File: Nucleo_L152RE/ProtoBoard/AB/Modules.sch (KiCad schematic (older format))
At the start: 30 parts, among them CON1 USB-MICRO-B, J2 EXT, P31 Ant, U4 S25FL127S, U5 MT3329_GPS, U6 RFM69HW

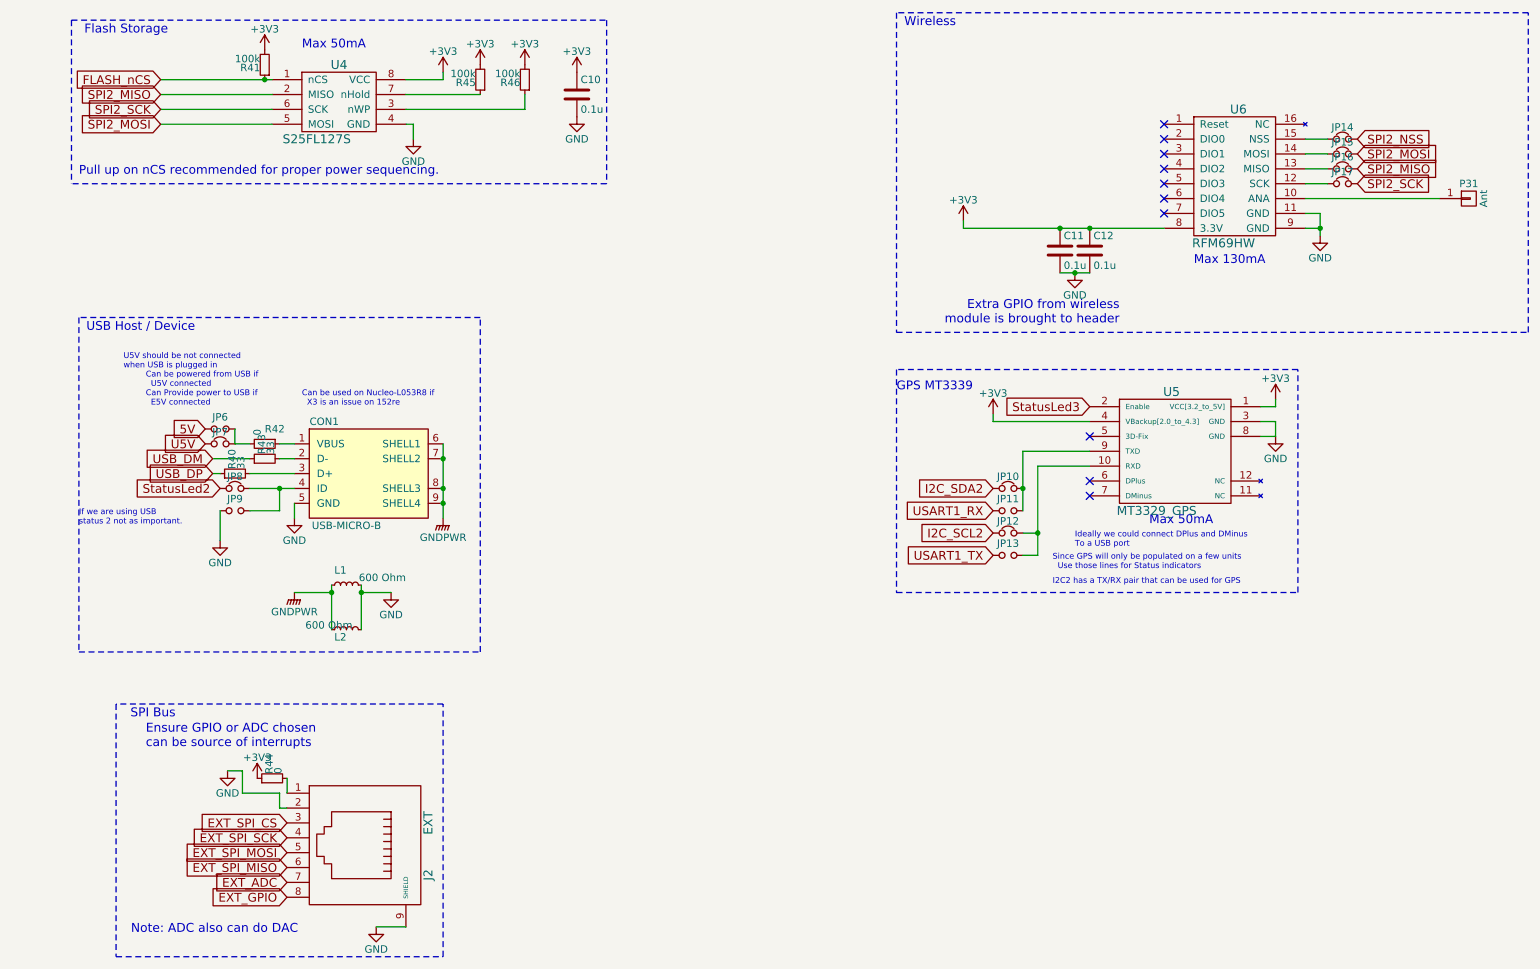
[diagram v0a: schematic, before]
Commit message: Components mostly laid out into final resting positions with exception of plethora of single pin connections for easily connecting to GND, 3.3V, 5V, 3.3Vctl.
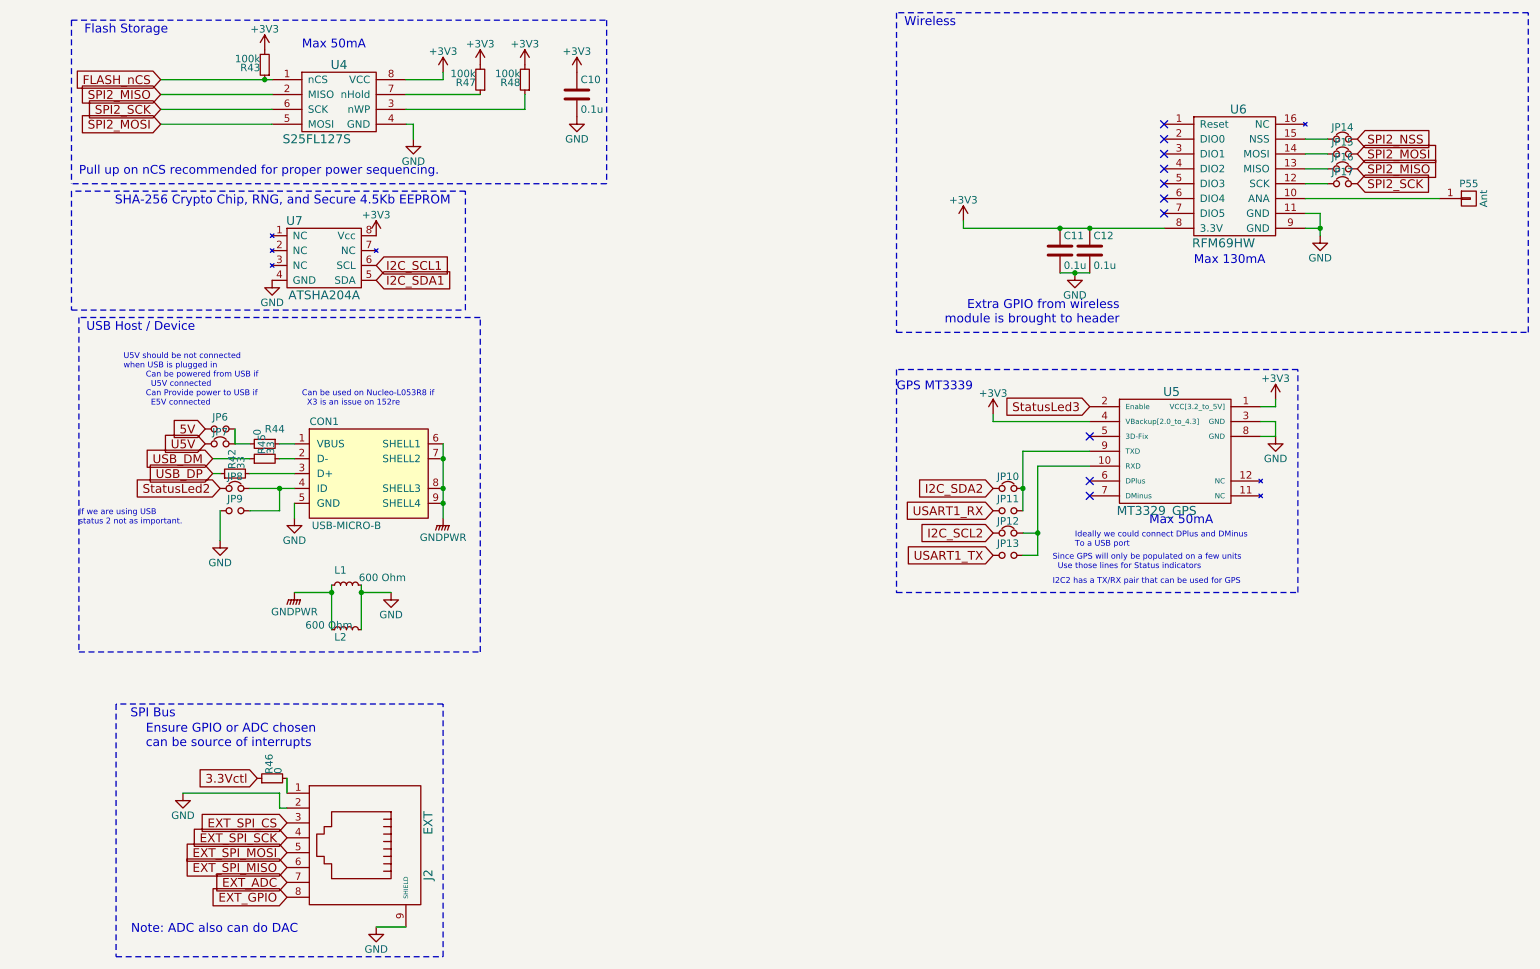
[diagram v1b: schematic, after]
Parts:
- added U7: ATSHA204A, nucleo:8-SOIC-JEDEC_MS-012AA, symbol ATSHA204A
- JP10, JP12, JP14, JP15, JP16, JP17, JP7, JP8: footprint nucleo:SB_NC -> nucleo:SB_NC_Smaller
- JP11, JP13, JP6, JP9: footprint nucleo:SB_NO -> nucleo:SB_NO_Smaller
- P55: renamed from P31; footprint Pin_Headers:Pin_Header_Straight_1x01 -> nucleo:Antenna_1pin
- U5: footprint nucleo:MT3329 -> nucleo:MT3329_LessPins
- U6: footprint nucleo:RFM69HW -> nucleo:RFM69HW_LessPins
- renumbered R40 to R42, R41 to R43, R42 to R44, R43 to R45, R44 to R46, R45 to R47, R46 to R48
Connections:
- net +3V3: now also U7.8 (Vcc); no longer R46.1
- net GND: now also U7.4 (GND)
- new net 3.3Vctl: R46.1
- new net I2C_SCL1: U7.6 (SCL)
- new net I2C_SDA1: U7.5 (SDA)
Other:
- note added: "SHA-256 Crypto Chip, RNG, and Secure 4.5Kb EEPROM"

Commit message: Added many traces which will have to be removed since I put via's on pads :/
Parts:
- JP10, JP12, JP14, JP15, JP16, JP17, JP7, JP8: footprint nucleo:SB_NC_Smaller -> nucleo:SB_NO_Smaller; symbol Jumper_NC_Small -> Jumper_Small
- JP11, JP13, JP6: symbol Jumper_NO_Small -> Jumper_Small
- JP9: value Jumper_NO_Small -> Jumper_Small; symbol Jumper_NO_Small -> Jumper_Small
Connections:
- net I2C_SCL2: now also JP12.2, JP13.2, U5.10 (RXD)
- net I2C_SDA2: now also JP10.2, JP11.2, U5.9 (TXD)
- net SPI2_MISO: now also JP16.1, U6.13 (MISO)
- net SPI2_MOSI: now also JP15.1, U6.14 (MOSI)
- net SPI2_NSS: now also JP14.1, U6.15 (NSS)
- net SPI2_SCK: now also JP17.1, U6.12 (SCK)
- net StatusLed2: now also CON1.4 (ID), JP8.2, JP9.2
- net U5V: now also JP6.2, JP7.2, R44.2
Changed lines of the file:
@@
 $EndComp
 $Comp
-L Jumper_NC_Small JP14
+L Jumper_Small JP14
 U 1 1 555AFD1A
 P 9250 1450
 F 0 "JP14" H 9250 1530 50  0000 C CNN
 F 1 "Jumper_NC_Small" H 9260 1390 50  0001 C CNN
-F 2 "nucleo:SB_NC_Smaller" H 9250 1450 60  0001 C CNN
+F 2 "nucleo:SB_NO_Smaller" H 9250 1450 60  0001 C CNN
 F 3 "" H 9250 1450 60  0000 C CNN
 	1    9250 1450
@@
 $EndComp
 $Comp
-L Jumper_NC_Small JP15
+L Jumper_Small JP15
 U 1 1 555AFD21
 P 9250 1550
 F 0 "JP15" H 9250 1630 50  0000 C CNN
 F 1 "Jumper_NC_Small" H 9260 1490 50  0001 C CNN
-F 2 "nucleo:SB_NC_Smaller" H 9250 1550 60  0001 C CNN
+F 2 "nucleo:SB_NO_Smaller" H 9250 1550 60  0001 C CNN
 F 3 "" H 9250 1550 60  0000 C CNN
 	1    9250 1550
@@
 $EndComp
 $Comp
-L Jumper_NC_Small JP16
+L Jumper_Small JP16
 U 1 1 555AFD28
 P 9250 1650
 F 0 "JP16" H 9250 1730 50  0000 C CNN
 F 1 "Jumper_NC_Small" H 9260 1590 50  0001 C CNN
-F 2 "nucleo:SB_NC_Smaller" H 9250 1650 60  0001 C CNN
+F 2 "nucleo:SB_NO_Smaller" H 9250 1650 60  0001 C CNN
 F 3 "" H 9250 1650 60  0000 C CNN
 	1    9250 1650
@@
 $EndComp
 $Comp
-L Jumper_NC_Small JP17
+L Jumper_Small JP17
 U 1 1 555AFD2F
 P 9250 1750
 F 0 "JP17" H 9250 1830 50  0000 C CNN
 F 1 "Jumper_NC_Small" H 9260 1690 50  0001 C CNN
-F 2 "nucleo:SB_NC_Smaller" H 9250 1750 60  0001 C CNN
+F 2 "nucleo:SB_NO_Smaller" H 9250 1750 60  0001 C CNN
 F 3 "" H 9250 1750 60  0000 C CNN
 	1    9250 1750
@@
 Connection ~ 9100 2050
 Wire Wire Line
-	9000 1450 9150 1450
-Wire Wire Line
-	9000 1550 9150 1550
-Wire Wire Line
-	9000 1650 9150 1650
-Wire Wire Line
-	9000 1750 9150 1750
+	9000 1450 9350 1450
+Wire Wire Line
+	9000 1550 9350 1550
+Wire Wire Line
+	9000 1650 9350 1650
+Wire Wire Line
+	9000 1750 9350 1750
 Wire Notes Line
 	6250 600  6250 2750
@@
 NoConn ~ 7550 3450
 $Comp
-L Jumper_NC_Small JP10
+L Jumper_Small JP10
 U 1 1 555B1CAF
 P 7000 3800
 F 0 "JP10" H 7000 3880 50  0000 C CNN
 F 1 "Jumper_NC_Small" H 7010 3740 50  0001 C CNN
-F 2 "nucleo:SB_NC_Smaller" H 7000 3800 60  0001 C CNN
+F 2 "nucleo:SB_NO_Smaller" H 7000 3800 60  0001 C CNN
 F 3 "" H 7000 3800 60  0000 C CNN
 	1    7000 3800
@@
 $EndComp
 $Comp
-L Jumper_NC_Small JP12
+L Jumper_Small JP12
 U 1 1 555B1CB6
 P 7000 4100
 F 0 "JP12" H 7000 4180 50  0000 C CNN
 F 1 "Jumper_NC_Small" H 7010 4040 50  0001 C CNN
-F 2 "nucleo:SB_NC_Smaller" H 7000 4100 60  0001 C CNN
+F 2 "nucleo:SB_NO_Smaller" H 7000 4100 60  0001 C CNN
 F 3 "" H 7000 4100 60  0000 C CNN
 	1    7000 4100
@@
 $EndComp
 $Comp
-L Jumper_NO_Small JP13
+L Jumper_Small JP13
 U 1 1 555B1CBD
 P 7000 4250
@@
 $EndComp
 $Comp
-L Jumper_NO_Small JP11
+L Jumper_Small JP11
 U 1 1 555B1CC4
 P 7000 3950
@@
 	7200 3650 7550 3650
 Wire Wire Line
-	7200 4100 7100 4100
+	6900 4100 7200 4100
 Connection ~ 7200 4100
 Wire Wire Line
@@
 $EndComp
 $Comp
-L Jumper_NC_Small JP8
+L Jumper_Small JP8
 U 1 1 555B24FC
 P 1800 3800
 F 0 "JP8" H 1800 3880 50  0000 C CNN
 F 1 "Jumper_NC_Small" H 1810 3740 50  0001 C CNN
-F 2 "nucleo:SB_NC_Smaller" H 1800 3800 60  0001 C CNN
+F 2 "nucleo:SB_NO_Smaller" H 1800 3800 60  0001 C CNN
 F 3 "" H 1800 3800 60  0000 C CNN
 	1    1800 3800
@@
 If we are using USB\nstatus 2 not as important.
 $Comp
-L Jumper_NO_Small JP9
+L Jumper_Small JP9
 U 1 1 555B2505
 P 1800 3950
 F 0 "JP9" H 1800 4030 50  0000 C CNN
-F 1 "Jumper_NO_Small" H 1810 3890 50  0001 C CNN
+F 1 "Jumper_Small" H 1810 3890 50  0001 C CNN
 F 2 "nucleo:SB_NO_Smaller" H 1800 3950 60  0001 C CNN
 F 3 "" H 1800 3950 60  0000 C CNN
@@
 $EndComp
 $Comp
-L Jumper_NO_Small JP6
+L Jumper_Small JP6
 U 1 1 555B250C
 P 1700 3400
@@
 $EndComp
 $Comp
-L Jumper_NC_Small JP7
+L Jumper_Small JP7
 U 1 1 555B2513
 P 1700 3500
 F 0 "JP7" H 1700 3580 50  0000 C CNN
 F 1 "Jumper_NC_Small" H 1710 3440 50  0001 C CNN
-F 2 "nucleo:SB_NC_Smaller" H 1700 3500 60  0001 C CNN
+F 2 "nucleo:SB_NO_Smaller" H 1700 3500 60  0001 C CNN
 F 3 "" H 1700 3500 60  0000 C CNN
 	1    1700 3500
@@
 	2100 3600 2200 3600
 Wire Wire Line
-	1900 3800 2200 3800
+	1700 3800 2200 3800
 Wire Wire Line
 	3200 3500 3200 4000
@@
 	1700 4150 1700 3950
 Wire Wire Line
-	1900 3950 2100 3950
-Wire Wire Line
 	2100 3950 2100 3800
 Connection ~ 2100 3800
@@
 	2100 3500 2200 3500
 Wire Wire Line
-	1800 3500 1900 3500
+	1600 3500 1900 3500
 Wire Wire Line
 	1800 3400 1800 3500
@@
 Wire Notes Line
 	3350 1800 700  1800
+Connection ~ 1900 3800
+Wire Wire Line
+	2100 3950 1900 3950
+Connection ~ 1800 3500
+Connection ~ 9150 1750
+Connection ~ 9150 1650
+Connection ~ 9150 1550
+Connection ~ 9150 1450
+Wire Wire Line
+	6900 3800 7100 3800
+Connection ~ 7100 4100
 $EndSCHEMATC

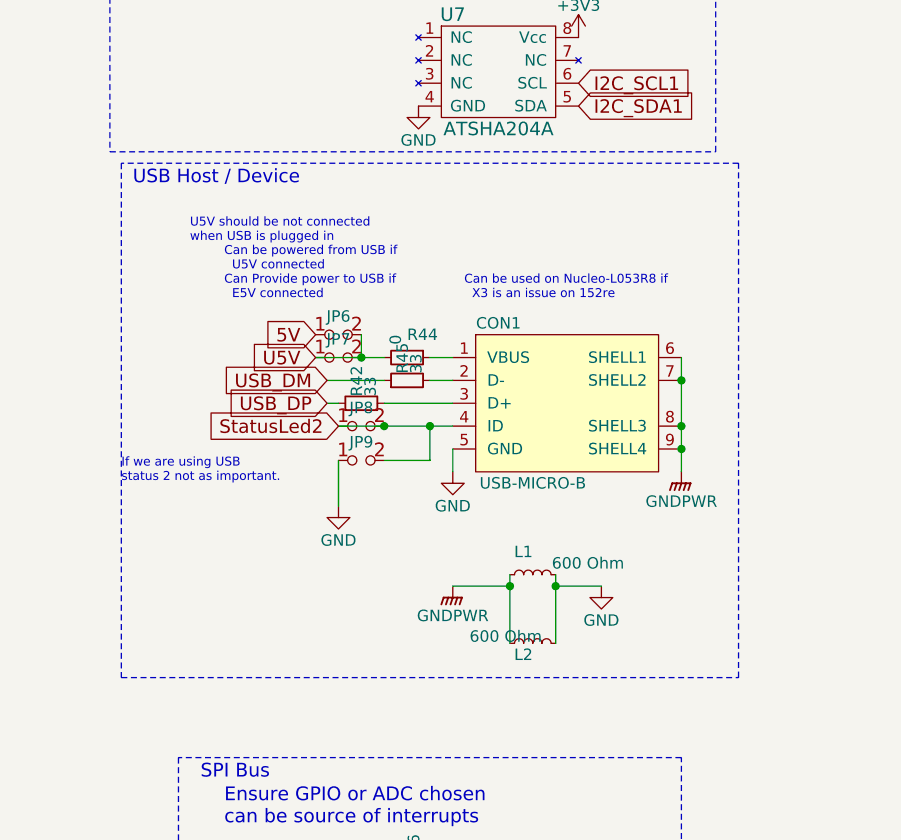
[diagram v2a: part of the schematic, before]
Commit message: Final draft with all traces and artwork in place.
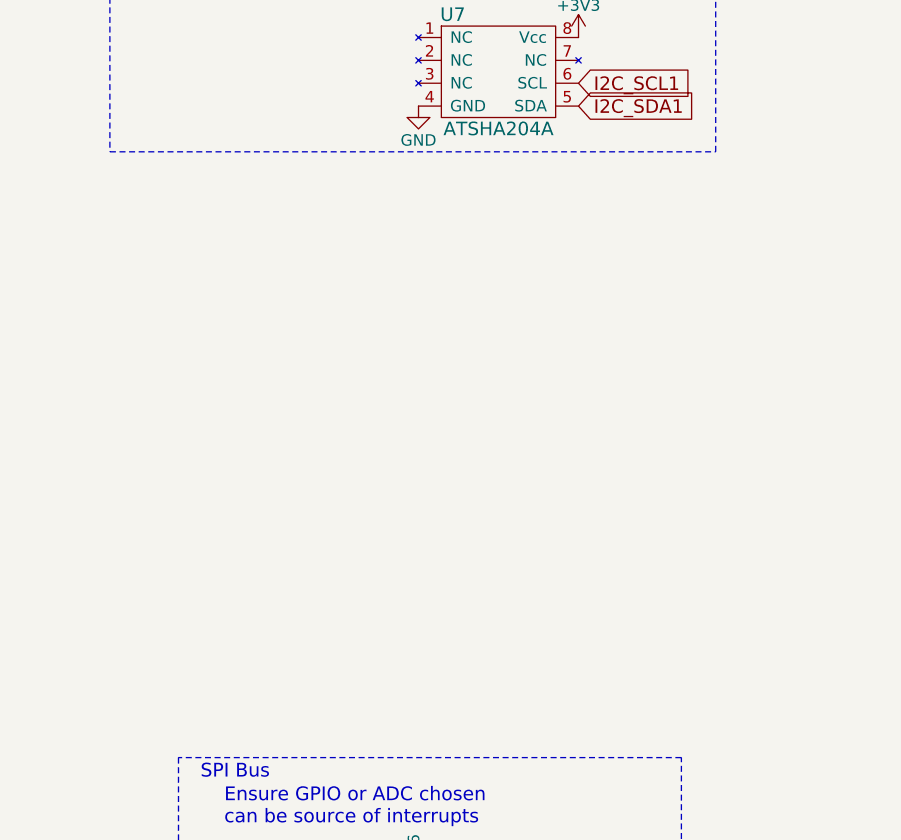
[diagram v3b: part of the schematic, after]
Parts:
- removed CON1: USB-MICRO-B, nucleo:USB_micro_AB, symbol USB-MICRO-B
- removed JP6: Jumper_NO_Small, nucleo:SB_NO_Smaller, symbol Jumper_Small
- removed JP7, JP8: Jumper_NC_Small, nucleo:SB_NO_Smaller, symbol Jumper_Small
- removed JP9: Jumper_Small, nucleo:SB_NO_Smaller, symbol Jumper_Small
- removed L1, L2: 600 Ohm, Resistors_SMD:R_0603_HandSoldering, symbol L_Small
- removed R42, R45: 33, Resistors_SMD:R_0603_HandSoldering, symbol R_Small
- removed R44: 0, Resistors_SMD:R_0603_HandSoldering, symbol R_Small
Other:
- note removed: "Can be powered from USB if\n U5V connected\nCan Provide power to USB if\n E5V connected"
- note removed: "Can be used on Nucleo-L053R8 if\n X3 is an issue on 152re"
- note removed: "If we are using USB\nstatus 2 not as important."
- note removed: "U5V should be not connected \nwhen USB is plugged in"
- note removed: "USB Host / Device"

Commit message: Updated MFG part numbers on schematic for BOM generation.
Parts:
- U7: MFG (none) -> ATSHA204A-SSHDA-B
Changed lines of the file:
@@
 F 2 "nucleo:8-SOIC-JEDEC_MS-012AA" H 2400 2250 59  0001 C CNN
 F 3 "" H 2400 2250 59  0000 C CNN
+F 4 "ATSHA204A-SSHDA-B" H 2400 2250 60  0001 C CNN "MFG"
 	1    2400 2250
 	1    0    0    -1
